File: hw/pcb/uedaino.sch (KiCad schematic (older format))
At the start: 27 parts, among them IC1 ATMEGA328P-A, P1 CN_PWR, P2 CN_UART, P3 ANALOG_IN, P5 POWER, P7 DIGITAL, SW1 SW_PUSH, SW2 SW_PWSEL, U1 AP1117

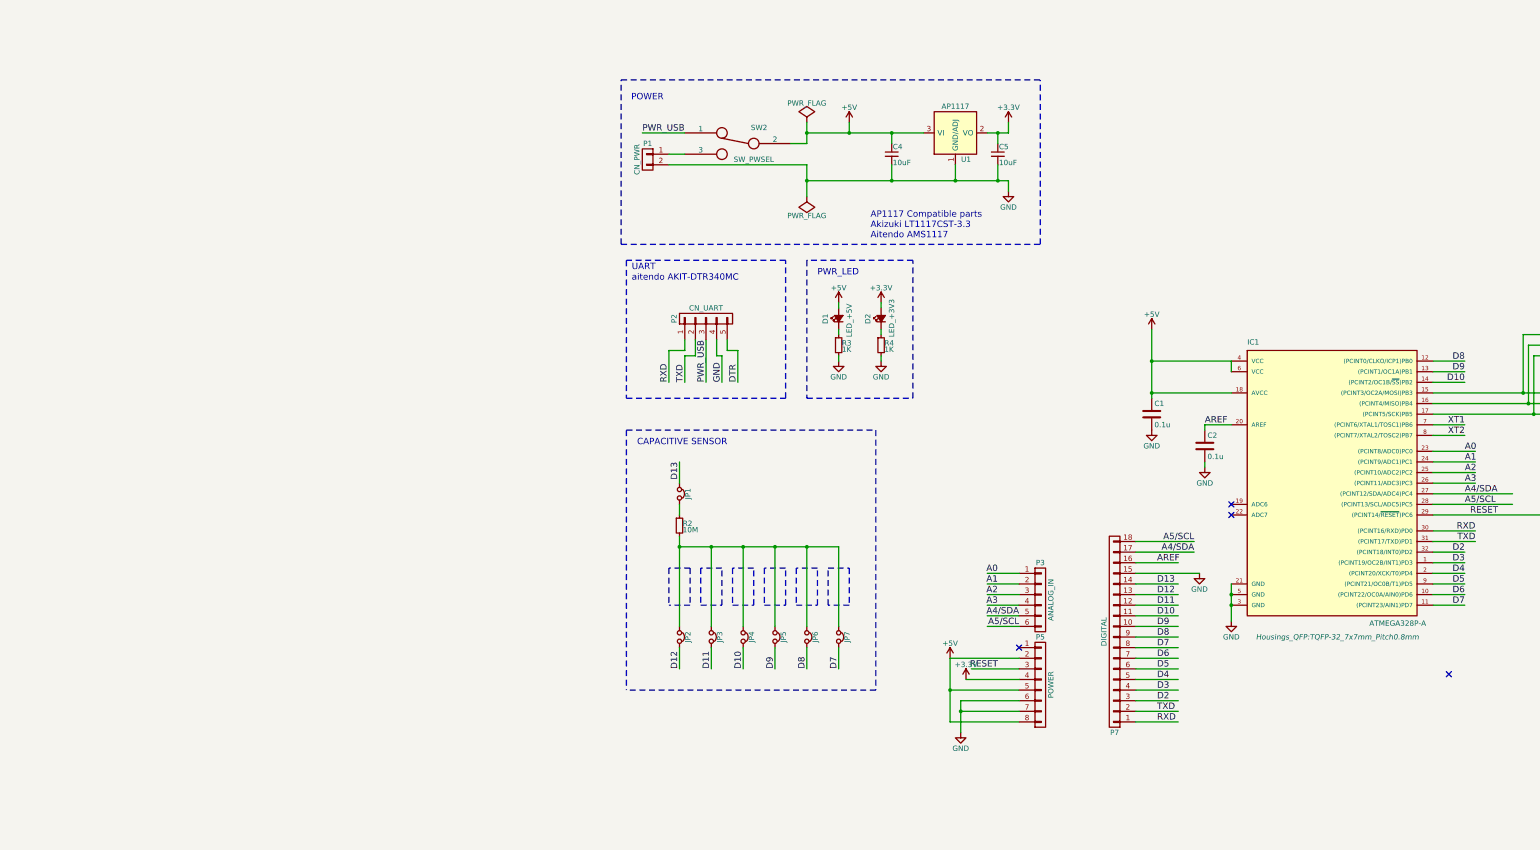
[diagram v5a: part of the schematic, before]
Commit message: Roughly placed the components
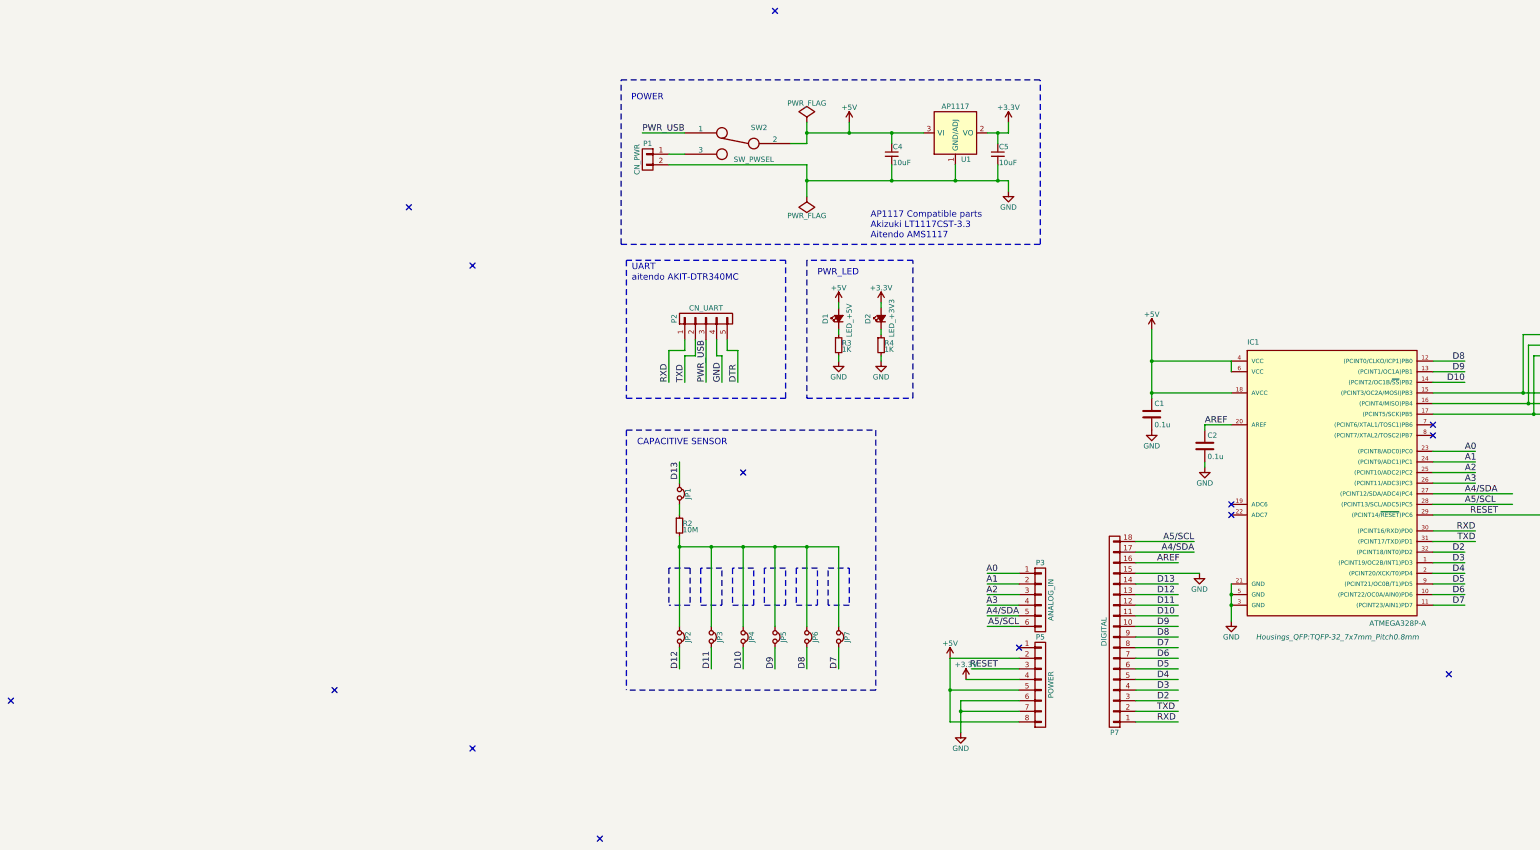
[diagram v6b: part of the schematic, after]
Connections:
- net labels removed: XT1, XT2
- wire segments 125 -> 123
- no-connect marks 4 -> 14
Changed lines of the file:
@@
 	1    0    0    -1
 $EndComp
-Text Label 8700 3800 2    60   ~ 0
-XT1
-Text Label 8700 3900 2    60   ~ 0
-XT2
 $Comp
 L CONN_01X02 P1
@@
 PWR_LED
 $Comp
-L +5V #PWR017
+L +5V #PWR015
 U 1 1 585D04F4
 P 9700 4100
-F 0 "#PWR017" H 9700 3950 50  0001 C CNN
+F 0 "#PWR015" H 9700 3950 50  0001 C CNN
 F 1 "+5V" H 9700 4240 50  0000 C CNN
 F 2 "" H 9700 4100 50  0000 C CNN
@@
 NoConn ~ 4500 5900
 $Comp
-L +5V #PWR021
+L +5V #PWR016
 U 1 1 5872286D
 P 3850 6000
-F 0 "#PWR021" H 3850 5850 50  0001 C CNN
+F 0 "#PWR016" H 3850 5850 50  0001 C CNN
 F 1 "+5V" H 3850 6140 50  0000 C CNN
 F 2 "" H 3850 6000 50  0000 C CNN
@@
 $EndComp
 $Comp
-L +3.3V #PWR022
+L +3.3V #PWR017
 U 1 1 587229CE
 P 4000 6200
-F 0 "#PWR022" H 4000 6050 50  0001 C CNN
+F 0 "#PWR017" H 4000 6050 50  0001 C CNN
 F 1 "+3.3V" H 4000 6340 50  0000 C CNN
 F 2 "" H 4000 6200 50  0000 C CNN
@@
 $EndComp
 $Comp
-L GND #PWR023
+L GND #PWR018
 U 1 1 58722F5E
 P 3950 6700
-F 0 "#PWR023" H 3950 6450 50  0001 C CNN
+F 0 "#PWR018" H 3950 6450 50  0001 C CNN
 F 1 "GND" H 3950 6550 50  0000 C CNN
 F 2 "" H 3950 6700 50  0000 C CNN
@@
 D13
 $Comp
-L GND #PWR024
+L GND #PWR019
 U 1 1 58727023
 P 6200 5200
-F 0 "#PWR024" H 6200 4950 50  0001 C CNN
+F 0 "#PWR019" H 6200 4950 50  0001 C CNN
 F 1 "GND" H 6200 5050 50  0000 C CNN
 F 2 "" H 6200 5200 50  0000 C CNN
@@
 Connection ~ 6500 5500
 Wire Wire Line
-	8400 3800 8700 3800
-Wire Wire Line
-	8400 3900 8700 3900
-Wire Wire Line
 	2500 1050 3600 1050
 Wire Wire Line
@@
 NoConn ~ 8550 6150
 NoConn ~ 6500 4550
+NoConn ~ 8400 3800
+NoConn ~ 8400 3900
+NoConn ~ 2200 -100
+NoConn ~ -1250 1750
+NoConn ~ 550  7700
+NoConn ~ -650 2300
+NoConn ~ 1900 4250
+NoConn ~ -650 6850
+NoConn ~ -5000 6400
+NoConn ~ -1950 6300
 $EndSCHEMATC
